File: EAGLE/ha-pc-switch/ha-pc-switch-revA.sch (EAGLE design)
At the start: 83 parts, among them J4 QWIIC_RIGHT_ANGLE, Q1 NPN, Q2 NPN, Q3 NPN, Q4 NPN, U1 STM8S001J3, U2 ILD213T, U3 ILD213T, U5 ILD213T, U6 ILD213T, U7 REG1117-3.3

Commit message: _
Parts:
- removed D3, D4: (no value), adafruit:DIODESOD-523
- added R33: 0R, rcl:R-EU_R0603
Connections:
- removed net N$10: D4.A, J3.1
- new net VXX: J3.1, R33.2, U1.VDD
- net VCC: now also R33.1; no longer D3.A
- net V_ISOL: no longer D3.C, D4.C, U1.VDD
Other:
- note added: "ISOLATE FOR PROGRAMMING"

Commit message: _
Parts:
- removed J1, J_HDD_LED_3, J_PC_ON_1, J_PC_ON_3, J_PWR_LED_1, J_PWR_LED_2, UNDEF_1, UNDEF_2: (no value), SparkFun-Connectors:CONN_021X02_NO_SILK
- removed J2: (no value), SparkFun-Connectors:CONN_05SCREW
- removed J4: QWIIC_RIGHT_ANGLE, ts_custom_nick_nacks:QWIIC_CONNECTORJS-1MM
- removed J_PC_ON_2, J_PWR_LED2: (no value), SparkFun-Connectors:CONN_02PTH3
- removed S1: (no value), ts_custom_nick_nacks:MOMENTARY-SWITCH-SPST-1
- removed U6: ILD213T, SparkFun:OPTOISOLATOR-2SOIC8
- added J_HDD_LED_2, J_MSG_LED_1, J_MSG_LED_2, J_NC_1, J_NC_2, J_PWR_1, J_PWR_2, RST: (no value), SparkFun-Connectors:CONN_021X02_NO_SILK
- added J_MSG_LED_3, J_PWR_3: (no value), SparkFun-Connectors:CONN_02PTH3
- added J_OPT: (no value), SparkFun-Connectors:CONN_05SCREW
- added J_QWIIC: QWIIC_RIGHT_ANGLE, ts_custom_nick_nacks:QWIIC_CONNECTORJS-1MM
- added S_RST: (no value), ts_custom_nick_nacks:MOMENTARY-SWITCH-SPST-1
- added TP1, TP2, TP3, TP4, TP5, TP6, TP7, TP8: TEST-POINT3X5, SparkFun-Connectors:TEST-POINT3X5
- added U$5: MOUNTINGHOLE3.0THIN, ts_custom_nick_nacks:MOUNTINGHOLE3.0THIN
- added U4: TLP3123, __untitled:TLP3123
- C1: value 470nF -> 100nF
- C2: value 100nF -> 470nF
- C3, C4: value 100nF -> 330uF
- C7, C9: value 330uF -> 100nF
- J_RESET_2: device SparkFun-Connectors:CONN_02PTH3 -> SparkFun-Connectors:CONN_021X02_NO_SILK
- J_RESET_3: device SparkFun-Connectors:CONN_021X02_NO_SILK -> SparkFun-Connectors:CONN_02PTH3
- R13, R15: value 10 -> 220R
- R14, R16: value 220R -> 10R
- R2: value 10K -> 220R
- R22: value 10K -> 0R
- R23: value 0R -> 10K
- R25: value 330R -> 0R
- R26: value 10K -> 330R
- R30: value 330R -> 10K
- R33: value 0R -> 330R
- R4: value 220R -> 10K
- U5: value ILD213T -> TLP3123; device SparkFun:OPTOISOLATOR-2SOIC8 -> __untitled:TLP3123
- renumbered J3 to STM8_SWIM
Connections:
- removed net V_ISOL: C2.1
- new net VDD: C4.1, C8.1, C9.1, D1-MINI.3V3, ESP-12F.VCC, ESP-PROG_2X3.2, J_OPT.3, J_QWIIC.2, R10.2, R11.2, R12.2, R20.2, R21.2, R22.1, R27.2, R28.2, R29.2, R3.2, R4.2, R5.2, R6.2, R9.2, TP2.1, U7.OUT
- net !X_PWR_LONG: now also R33.1, TP8.1; no longer R32.1
- net !X_PWR_SHRT: now also R25.2, R28.1, TP4.1; no longer R23.2, R27.1
- net !X_RST_SHRT: now also TP5.1
- net 5VIN: now also R2.1; no longer R4.1
- net D1_SCL: now also J_OPT.5, J_QWIIC.4; no longer J2.5, J4.4
- net D2_SDA: now also J_OPT.4, J_QWIIC.3; no longer J2.4, J4.3
- net ESP_EN: now also R27.1; no longer R26.1
- net ESP_IO0: now also R29.1, R33.2; no longer R28.1, R32.2
- net GND: now also C3.2, C4.2, J_OPT.2, J_QWIIC.1, R23.1, R24.1, R30.1, RST.2, S_RST.3, TP3.1, U4.C, U5.C; no longer C6.2, C7.2, J1.2, J2.2, J4.1, R21.1, R22.1, R29.1, S1.3, U5.C1, U5.C2, U6.C1, U6.C2
- net HDD_LED+: now also J_HDD_LED_2.1; no longer J_HDD_LED_3.1
- net HDD_LED-: now also J_HDD_LED_2.2; no longer J_HDD_LED_3.2
- net N$14: now also R26.2; no longer R25.2
- net N$15: now also R32.2; no longer R31.2
- net N$16: now also R31.2; no longer R30.2
- net N$2: now also R2.2; no longer R4.2
- net N$24: now also C2.1; no longer C1.1
- net N$3: now also J_NC_1.1, J_NC_2.1; no longer UNDEF_1.1, UNDEF_2.1
- net N$4: now also J_NC_1.2, J_NC_2.2; no longer UNDEF_1.2, UNDEF_2.2
- net N$5: now also R15.2, U5.A; no longer R14.2, U5.A1, U5.A2
- net N$7: now also C6.1, R14.1; no longer C3.1, R13.1
- net N$8: now also C7.1, R16.1; no longer C4.1, R15.1
- net N$9: now also R13.2, U4.A; no longer R16.2, U6.A1, U6.A2
- net OUT1N: now also R3.1; no longer R2.1
- net OUT1N1: now also Q3.B; no longer Q4.B
- net OUT2N: now also R4.1; no longer R5.1
- net OUT2N1: now also Q4.B; no longer Q3.B
- net PC_ON+: now also J_PWR_1.1, J_PWR_2.1, J_PWR_3.1, R14.2, U4.D1; no longer J_PC_ON_1.1, J_PC_ON_2.1, J_PC_ON_3.1, R13.2, U5.CL1, U5.EM2
- net PC_ON-: now also C6.2, J_PWR_1.2, J_PWR_2.2, J_PWR_3.2, U4.D2; no longer C3.2, J_PC_ON_1.2, J_PC_ON_2.2, J_PC_ON_3.2, U5.CL2, U5.EM1
- net PWR_LED+: now also J_MSG_LED_1.1, J_MSG_LED_2.1, J_MSG_LED_3.1; no longer J_PWR_LED2.2, J_PWR_LED_1.1, J_PWR_LED_2.2
- net PWR_LED-: now also J_MSG_LED_1.2, J_MSG_LED_2.2, J_MSG_LED_3.2; no longer J_PWR_LED2.1, J_PWR_LED_1.2, J_PWR_LED_2.1
- net RESET+: now also R16.2, U5.D1; no longer R15.2, U6.CL1, U6.EM2
- net RESET-: now also C7.2, U5.D2; no longer C4.2, U6.CL2, U6.EM1
- net RST: now also R21.1, R26.1, RST.1, S_RST.1; no longer J1.1, R24.1, R25.1, S1.1
- net RX: now also R32.1; no longer R31.1
- net SWIM: now also R25.1; no longer R23.1
- net S_5VIN: now also R5.1; no longer R6.1
- net S_HDD_LED: now also Q4.C; no longer Q3.C
- net S_PWR_LED: now also Q3.C; no longer Q4.C
- net S_PWR_OK: now also R30.2, R6.1; no longer R29.2, R3.1
- net TX: now also R31.1; no longer R30.1
- net T_PWR_SWT: now also R13.1, R23.2, TP6.1; no longer R14.1, R21.2
- net T_RST_SWT: now also R15.1, R24.2, TP7.1; no longer R16.1, R22.2
- net VCC: now also C3.1, J_OPT.1, TP1.1; no longer C6.1, C7.1, C8.1, C9.1, D1-MINI.3V3, ESP-12F.VCC, ESP-PROG_2X3.2, J2.1, J2.3, J4.2, R10.2, R11.2, R12.2, R2.2, R20.2, R24.2, R26.2, R27.2, R28.2, R3.2, R33.1, R5.2, R6.2, R9.2, U7.OUT
- net VXX: now also C1.1, R22.2; no longer R33.2
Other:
- note added: "5V POWER SOURCE"
- note added: "Common rest button"
- note added: "Optioal IO / Expansion headers"
- moved on the sheet: C1, C2, C5, C8, C9, D1, D2, J_HDD_LED_1, J_RESET_1, J_RESET_2, J_RESET_3, Q1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

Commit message: _
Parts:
- removed STM8_SWIM: (no value), SparkFun-Connectors:CONN_04POLAR
- removed TP4, TP5, TP6, TP7, TP8: TEST-POINT3X5, SparkFun-Connectors:TEST-POINT3X5
- added C10, C11: 12pF, rcl:C-EUC0603
- added D3, D4: GREEN, SparkFun-LED:LED-GREEN0603
- added J1: 1X04_SMD_STRAIGHT_COMBO, SparkFun-Connectors:CONN_04SMD_STRAIGHT_COMBO
- added R34: 1K, rcl:R-EU_R0603
- added TP10, TP11, TP12, TP14, TP15, TP16, TP9: TEST-POINT3X5, SparkFun-Connectors:TEST-POINT3X5
- added U$15, U$16: FIDUCIAL, adafruit:FIDUCIAL
- added U$20: ARGB, __temp_to_delete:ARGB
- added U$21: 74AHCT1G125GW, ts_keyboards:74AHCT1G125GW
- added U$22: JUMPER-1X3-CLOSED-2, ts_jumpers:JUMPER-1X3-CLOSED-2
- added U$4: NUCLEO_HEADER, stm32c0:NUCLEO_HEADER
- added Y1: 32.768kHz, SparkFun-Clocks:CRYSTAL-32.768KHZSMD-3.2X1.5
- C1: device rcl:C-EUC0805 -> rcl:C-EUC0603
- C2: value 470nF -> 4.7uF; device rcl:C-EUC0805 -> rcl:C-EUC0603
- R21: value 10K -> 220R
- R22: value 0R -> 470R
- R25: value 0R -> 1K
- U1: value STM8S001J3 -> STM32C011FTSSOP20_STM-M; device __untitled:STM8S001J3 -> stm32c0:STM32C011FTSSOP20_STM-M
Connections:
- removed net D1_SCL: D1-MINI.D1, ESP-12F.5, J_OPT.5, J_QWIIC.4
- removed net D2_SDA: D1-MINI.D2, ESP-12F.4, J_OPT.4, J_QWIIC.3
- removed net N$24: C2.1, U1.VCAP
- removed net RX: D1-MINI.RX, ESP-PROG_2X3.5, R32.1
- removed net SWIM: R25.1, STM8_SWIM.2
- removed net VXX: C1.1, R22.2, STM8_SWIM.1, U1.VDD
- new net A0: D1-MINI.A0, ESP-12F.ADC, TP12.1
- new net CTS2: U1.PA11[PA9]
- new net D1/SCL: D1-MINI.D1, ESP-12F.5, J_OPT.5, J_QWIIC.4, R23.1, U1.PB6
- new net D2/SDA: D1-MINI.D2, ESP-12F.4, J_OPT.4, J_QWIIC.3, R24.1, U1.PB7
- new net IO10: ESP-12F.10, TP15.1
- new net IO11: ESP-12F.11, TP14.1
- new net IO16: ESP-12F.16
- new net IO6: ESP-12F.6, TP11.1
- new net IO7: ESP-12F.7, TP10.1
- new net IO8: ESP-12F.8, TP9.1
- new net IO9: ESP-12F.9, TP16.1
- new net N$10: C10.1, U1.PC14-OSCX_IN, Y1.2
- new net N$11: C11.1, U1.PC15-OSCX_OUT, Y1.1
- new net N$12: R21.2, U$21.A_DIN
- new net N$17: R22.1, U$21.Y_DOUT
- new net N$18: R22.2, U$20.D
- new net N$19: D3.A, R25.1
- new net N$20: R23.2, U$22.2
- new net N$21: R24.2, U$22.1
- new net N$25: D4.A, R34.1
- new net RESET: U$4.NC, U1.PF2-NRST
- new net RTS2: U1.PA12[PA10]
- new net RX/RGB: D1-MINI.RX, ESP-PROG_2X3.5, R21.1, R32.1, U1.PA8
- new net RX2: U1.PA1
- new net SWCLK: J1.2, U$4.SWCLK, U1.PA14-BOOT0
- new net SWDIO: J1.3, U$4.SWDIO, U1.PA13
- new net TX2: U1.PA0
- new net WAKE: U1.PA4
- net !X_PWR_LONG: now also U1.PA5; no longer TP8.1, U1.D6_A1_RX
- net !X_PWR_SHRT: now also U1.PA6; no longer R25.2, TP4.1, U1.D5_D3_D1_C6_TX
- net !X_RST_SHRT: now also U1.PA7; no longer TP5.1, U1.C5_C4_C3
- net GND: now also C10.2, C11.2, D3.C, D4.C, J1.1, U$20.G, U$21.!OE, U$21.3_GND, U$4.GND, U1.VSS/VSSA; no longer R23.1, R24.1, STM8_SWIM.3, U1.VSS_GND
- net RST: no longer R21.1, STM8_SWIM.4
- net T_PWR_SWT: now also R25.2, U1.PA3; no longer R23.2, TP6.1, U1.B4_SCL
- net T_RST_SWT: now also R34.2, U1.PA2; no longer R24.2, TP7.1, U1.B5_SDA
- net VCC: now also C1.1, C2.1, J1.4, U$20.V, U$21.5_VCC, U$22.3, U$4.3V3, U1.VDD/VDDA
- net VDD: no longer R21.2, R22.1
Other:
- note added: "ARGB Feature"
- note added: "DO NOT POPULATE (Only to be used if not using a D1 Mini)"
- note added: "I2C Pull-ups"
- note added: "STM32C011Fx Relay "On-Shot" Delay-OFF Timer"
- note removed: "DO NOT POPULATE"
- note removed: "ISOLATE FOR PROGRAMMING"
- note removed: "Place near VDD pin"
- note removed: "Pulled up by D1-Mini"
- note removed: "Pulled up by Pull-up R20"
- note removed: "STM8S001J3 Relay "On-Shot" Delay-OFF Timer"
- note removed: "SWIM"
- note removed: "SWIM PROGRAMMING HEADER [DNP]"
- moved on the sheet: C1, C2, C3, C4, C5, D1-MINI, R20, R23, R24, RST, S_RST, U7

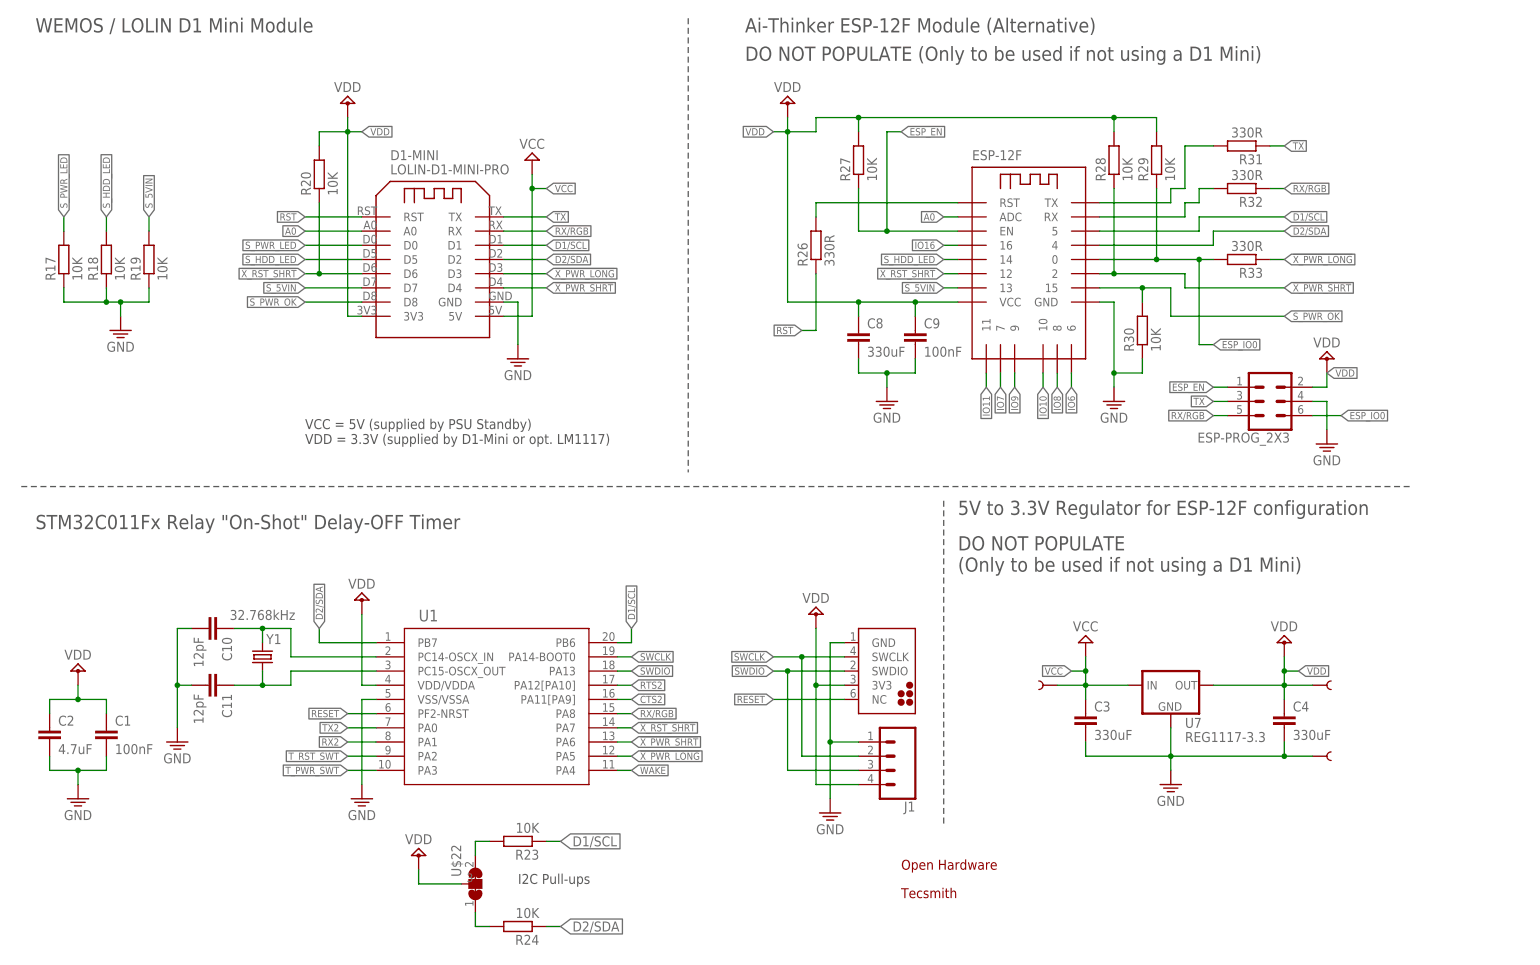
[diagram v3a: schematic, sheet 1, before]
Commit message: pcb routed
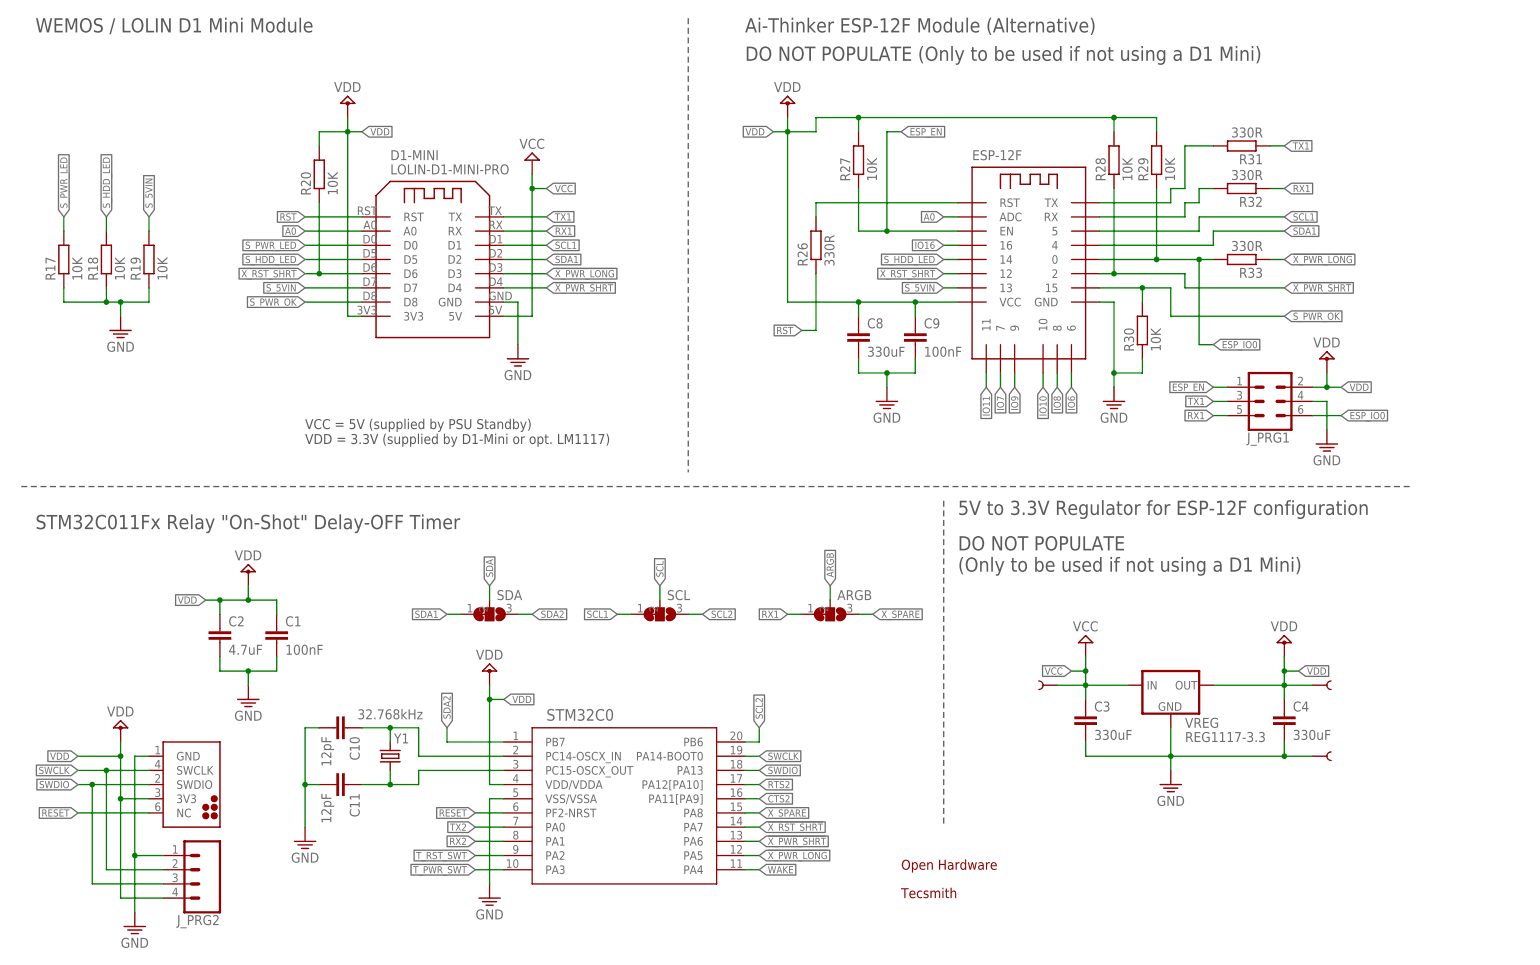
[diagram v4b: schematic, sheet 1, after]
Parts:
- removed J1: 1X04_SMD_STRAIGHT_COMBO, SparkFun-Connectors:CONN_04SMD_STRAIGHT_COMBO
- removed J_OPT: (no value), SparkFun-Connectors:CONN_05SCREW
- removed R21: 220R, rcl:R-EU_R0603
- removed U$20: ARGB, __temp_to_delete:ARGB
- removed U$22: JUMPER-1X3-CLOSED-2, ts_jumpers:JUMPER-1X3-CLOSED-2
- removed U$4: NUCLEO_HEADER, stm32c0:NUCLEO_HEADER
- removed U1: STM32C011FTSSOP20_STM-M, stm32c0:STM32C011FTSSOP20_STM-M
- added ARGB, SCL, SDA: JUMPER-1X3-CLOSED, ts_jumpers:JUMPER-1X3-CLOSED
- added I2C: JUMPER-1X3-CLOSED-2, ts_jumpers:JUMPER-1X3-CLOSED-2
- added J_ARGB: ARGB, __temp_to_delete:ARGB
- added J_DBG2: NUCLEO_HEADER, stm32c0:NUCLEO_HEADER
- added J_I2C: (no value), SparkFun-Connectors:CONN_05SCREW
- added J_PRG2: 1X04_SMD_STRAIGHT_COMBO, SparkFun-Connectors:CONN_04SMD_STRAIGHT_COMBO
- added STM32C0: STM32C011FTSSOP20_STM-M, stm32c0:STM32C011FTSSOP20_STM-M
- renumbered D3 to LED1, D4 to LED2, ESP-PROG_2X3 to J_PRG1, U$21 to LSHFT, U2 to OC_PWR, U3 to OC_LED, U4 to RL_PWR, U5 to RL_RST, U7 to VREG
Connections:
- net TX renamed TX1
- removed net D1/SCL: D1-MINI.D1, ESP-12F.5, J_OPT.5, J_QWIIC.4, R23.1, U1.PB6
- removed net D2/SDA: D1-MINI.D2, ESP-12F.4, J_OPT.4, J_QWIIC.3, R24.1, U1.PB7
- removed net N$12: LSHFT.A_DIN, R21.2
- removed net RX/RGB: D1-MINI.RX, J_PRG1.5, R21.1, R32.1, U1.PA8
- new net ARGB: ARGB.2, LSHFT.A_DIN
- new net RX1: ARGB.1, D1-MINI.RX, J_PRG1.5, R32.1
- new net SCL: J_I2C.5, J_QWIIC.4, R23.1, SCL.2
- new net SCL1: D1-MINI.D1, ESP-12F.5, SCL.1
- new net SCL2: SCL.3, STM32C0.PB6
- new net SDA: J_I2C.4, J_QWIIC.3, R24.1, SDA.2
- new net SDA1: D1-MINI.D2, ESP-12F.4, SDA.1
- new net SDA2: SDA.3, STM32C0.PB7
- new net X_SPARE: ARGB.3, STM32C0.PA8
- net !X_PWR_LONG: now also STM32C0.PA5; no longer U1.PA5
- net !X_PWR_SHRT: now also STM32C0.PA6; no longer U1.PA6
- net !X_RST_SHRT: now also STM32C0.PA7; no longer U1.PA7
- net CTS2: now also STM32C0.PA11[PA9]; no longer U1.PA11[PA9]
- net GND: now also J_ARGB.G, J_DBG2.GND, J_I2C.2, J_PRG2.1, STM32C0.VSS/VSSA; no longer J1.1, J_OPT.2, U$20.G, U$4.GND, U1.VSS/VSSA
- net N$10: now also STM32C0.PC14-OSCX_IN; no longer U1.PC14-OSCX_IN
- net N$11: now also STM32C0.PC15-OSCX_OUT; no longer U1.PC15-OSCX_OUT
- net N$18: now also J_ARGB.D; no longer U$20.D
- net N$20: now also I2C.3; no longer U$22.2
- net N$21: now also I2C.1; no longer U$22.1
- net RESET: now also J_DBG2.NC, STM32C0.PF2-NRST; no longer U$4.NC, U1.PF2-NRST
- net RTS2: now also STM32C0.PA12[PA10]; no longer U1.PA12[PA10]
- net RX2: now also STM32C0.PA1; no longer U1.PA1
- net SWCLK: now also J_DBG2.SWCLK, J_PRG2.2, STM32C0.PA14-BOOT0; no longer J1.2, U$4.SWCLK, U1.PA14-BOOT0
- net SWDIO: now also J_DBG2.SWDIO, J_PRG2.3, STM32C0.PA13; no longer J1.3, U$4.SWDIO, U1.PA13
- net TX2: now also STM32C0.PA0; no longer U1.PA0
- net T_PWR_SWT: now also STM32C0.PA3; no longer U1.PA3
- net T_RST_SWT: now also STM32C0.PA2; no longer U1.PA2
- net VCC: now also J_ARGB.V, J_I2C.1; no longer C1.1, C2.1, J1.4, J_OPT.1, U$20.V, U$22.3, U$4.3V3, U1.VDD/VDDA
- net VDD: now also C1.1, C2.1, I2C.2, J_DBG2.3V3, J_I2C.3, J_PRG2.4, STM32C0.VDD/VDDA; no longer J_OPT.3
- net WAKE: now also STM32C0.PA4; no longer U1.PA4
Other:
- note added: "Optional IO / Expansion headers"
- note removed: "Optioal IO / Expansion headers"
- moved on the sheet: C1, C10, C11, C2, J_QWIIC, R22, Y1

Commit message: _
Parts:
- added J_RGB_5V: JUMPER-1X3-CLOSEDPINS, ts_jumpers:JUMPER-1X3-CLOSEDPINS
- added TP4: TEST-POINT3X5, SparkFun-Connectors:TEST-POINT3X5
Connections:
- new net N$12: J_ARGB.V, J_RGB_5V.2, LSHFT.5_VCC
- net 5VIN: now also J_RGB_5V.1
- net VCC: now also J_RGB_5V.3; no longer J_ARGB.V, LSHFT.5_VCC
- net WAKE: now also TP4.1
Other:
- moved on the sheet: J_ARGB, LSHFT, R22
